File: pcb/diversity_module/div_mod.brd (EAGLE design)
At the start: 40.9 x 28.7 mm, 4 parts

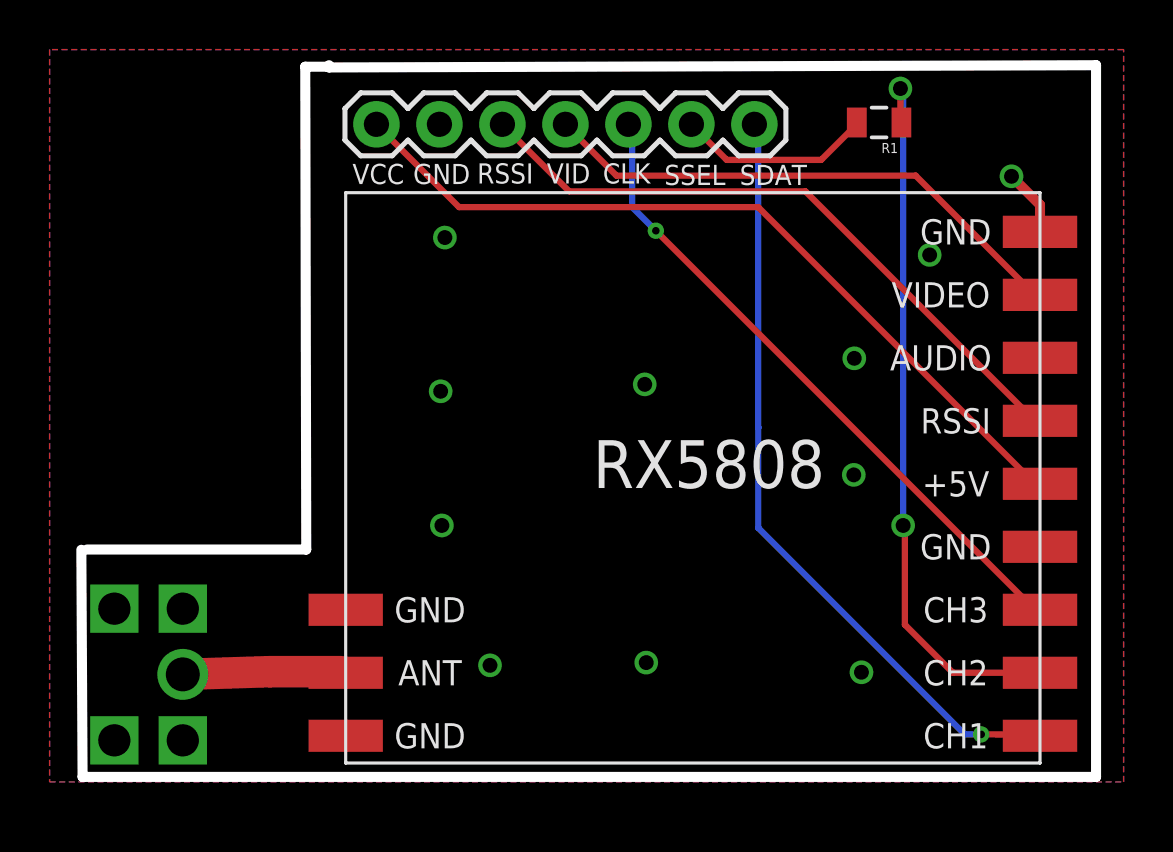
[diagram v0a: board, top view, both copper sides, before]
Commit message: regulator, buffer and new SMA connetor. v1.1
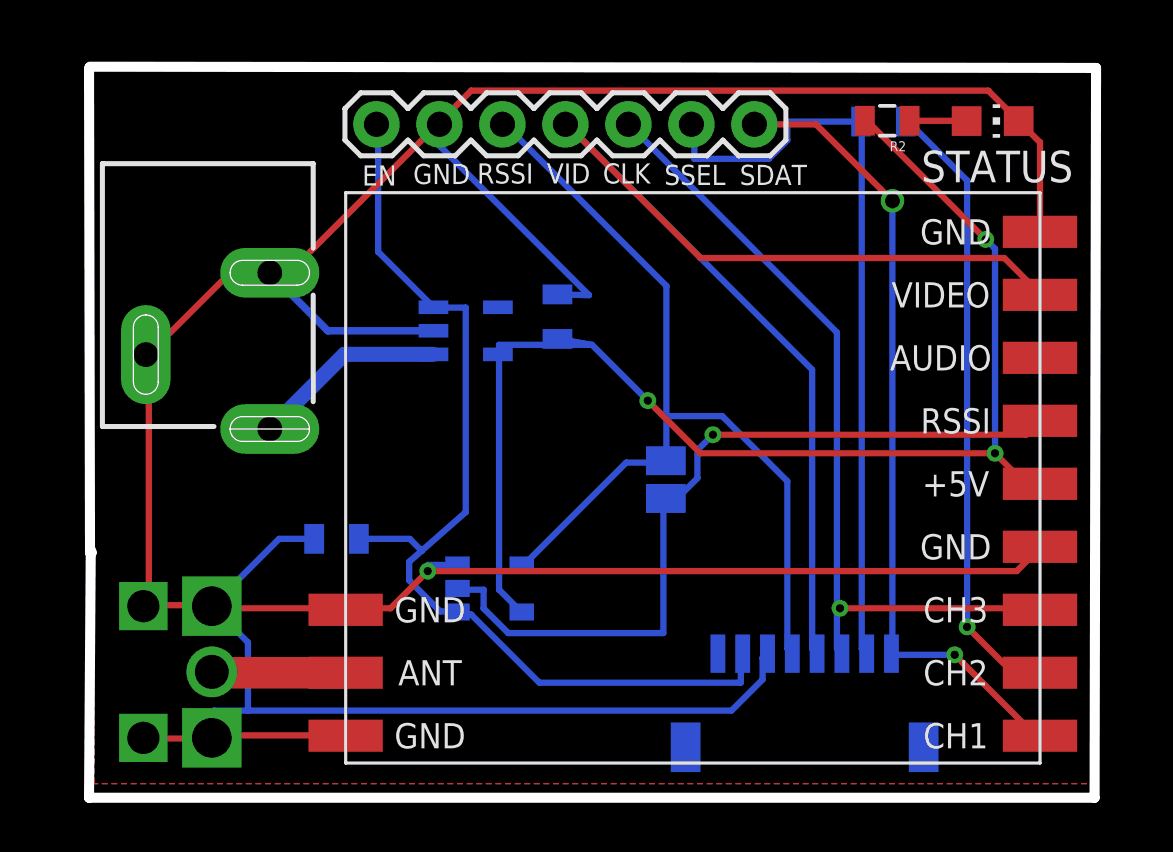
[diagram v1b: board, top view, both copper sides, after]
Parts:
- added C1: 0.1uf, SparkFun-Capacitors:0805
- added IC1: TPS77050, texas:SOT23-DBV
- added IC2: 74AHC1G126DBV, 74xx-little-de:SOT23-5
- added JP1: POWER_JACKSLT, SparkFun-Connectors:POWER_JACK_SLOT
- added R2: (no value), SparkFun-Passives:0805
- added R3: 10k, SparkFun-Passives:0805
- added SJ2: (no value), jumper:SJ
- added STATUS: (no value), led:CHIP-LED0805
- added U$3: EB-85ASMD, SparkFun-Connectors:EB-85A
- moved U$1 1.17 mm to (6.52, 4.41)
- moved R1 0.18 mm to (33.6, 26.6), flipped to the bottom, turned to 0 degrees
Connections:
- new net BATT: U$3.8
- new net ENABLE: IC1.3, IC2.1, JP3.7, R3.2, U$3.7
- new net N$2: R2.1, STATUS.A
- new net RSSI_MOD: IC2.2, RECEIVER_A.RSSI, SJ2.1
- new net VIN_UNREG: IC1.1, JP1.PWR
- net 5V: now also C1.1, IC1.5, IC2.5, R2.2; no longer JP3.7
- net GND: now also C1.2, IC1.2, IC2.3, JP1.GND@1, JP1.GND@2, R3.1, STATUS.C, U$3.6
- net RSSI_B: now also IC2.4, SJ2.2, U$3.5; no longer RECEIVER_A.RSSI
- net RXVIDOUT2: now also U$3.4
- net SPI_CLK: now also U$3.3
- net SPI_DATA: now also U$3.1
- net SPI_SEL_B: now also U$3.2
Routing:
- net GND: track 2.96 -> 155.5 mm, vias 11 -> 1
- net ENABLE: track 0.00 -> 40.7 mm
- net RSSI_MOD: track 0.00 -> 32.6 mm, vias 0 -> 1
- net RXVIDOUT2: track 22.0 -> 47.6 mm
- net SPI_SEL_B: track 7.92 -> 30.8 mm
- net 5V: track 32.8 -> 53.6 mm, vias 0 -> 3
- net RSSI_B: track 26.6 -> 36.9 mm
- net VIN_UNREG: track 0.00 -> 7.85 mm
- net SPI_CLK: track 26.6 -> 33.1 mm
- net N$1: track 29.3 -> 25.2 mm, vias 2 -> 1
- net N$2: track 0.00 -> 2.30 mm
- net SPI_DATA: track 31.2 -> 32.5 mm, vias 1 -> 2
- net N$5: track 6.58 -> 5.41 mm
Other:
- board size 40.9 x 28.7 mm -> 40.6 x 29.5 mm
- board text added: "EN"
- board text added: "buffer_bypass"
- board text added: "mikym0use diversity module v2 part of JAFar project"
- board text removed: "VCC"

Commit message: LDO name replaced
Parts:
- IC1: value TPS77050 -> REG113
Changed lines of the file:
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@@
 <grid distance="0.00999999999" unitdist="mm" unit="mm" style="lines" multiple="1" display="yes" altdistance="0.00500000001" altunitdist="mm" altunit="mm"/>
 <layers>
-<layer number="1" name="Top" color="4" fill="1" visible="yes" active="yes"/>
+<layer number="1" name="Top" color="4" fill="1" visible="no" active="yes"/>
 <layer number="16" name="Bottom" color="1" fill="1" visible="yes" active="yes"/>
 <layer number="17" name="Pads" color="2" fill="1" visible="yes" active="yes"/>
@@
 <attribute name="VALUE" x="24.02" y="3.84" size="1.27" layer="28" rot="MR0"/>
 </element>
-<element name="IC1" library="texas" package="SOT23-DBV" value="TPS77050" x="16.78" y="18.19" smashed="yes" rot="MR90">
-<attribute name="OC_FARNELL" value="1412883" x="16.78" y="18.19" size="1.778" layer="28" rot="MR90" display="off"/>
-<attribute name="OC_NEWARK" value="77C1189" x="16.78" y="18.19" size="1.778" layer="28" rot="MR90" display="off"/>
-<attribute name="MF" value="TEXAS INSTRUMENT CONNECTORS" x="16.78" y="18.19" size="1.778" layer="28" rot="MR90" display="off"/>
-<attribute name="MPN" value="TPS77050DBVT" x="16.78" y="18.19" size="1.778" layer="28" rot="MR90" display="off"/>
+<element name="IC1" library="texas" package="SOT23-DBV" value="REG113" x="16.78" y="18.19" smashed="yes" rot="MR90">
 <attribute name="VALUE" x="19.735" y="20.311" size="1.27" layer="28" rot="MR0"/>
 </element>

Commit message: diversity module v2.0
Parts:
- removed IC1: REG113, texas:SOT23-DBV
- removed IC2: 74AHC1G126DBV, 74xx-little-de:SOT23-5
- removed STATUS: (no value), led:CHIP-LED0805
- added C2: 1uf, SparkFun-Capacitors:0805
- added IC3: OPA336N, burr-brown:SOT23-5
- added JP2: (no value), SparkFun-Connectors:1X02_LOCK
- added SJ1: (no value), jumper:SJ
- added STAT: (no value), led:CHIP-LED0805
- added V1: LP38692P, lp38692:TO252-51
- C1: value 0.1uf -> 1uf
- JP1: value POWER_JACKSLT -> 5.5x2.1mm Barrel; device SparkFun-Connectors:POWER_JACK_SLOT -> SparkFun-Connectors:POWER_JACK_SMD
- moved JP1 24.0 mm to (34.8, 22.4), flipped to the bottom, turned to 270 degrees
- moved R3 13.3 mm to (13.6, 23.0), turned to 0 degrees
- moved SJ2 10.7 mm to (20.9, 2.22), turned to 180 degrees
- moved R1 7.14 mm to (40.7, 25.7), turned to 90 degrees
- moved C1 5.04 mm to (15.7, 20.3), turned to 270 degrees
- moved R2 1.71 mm to (32.1, 27.1), turned to 0 degrees
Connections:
- net 5V: now also IC3.5, SJ1.2, V1.OUT; no longer IC1.5, IC2.5
- net ENABLE: now also SJ1.1, V1.EN; no longer IC1.3, IC2.1
- net GND: now also C2.2, IC3.2, JP1.GND, JP1.P$4, JP2.1, STAT.C, V1.GND; no longer IC1.2, IC2.3, JP1.GND@1, JP1.GND@2, STATUS.C
- net N$2: now also STAT.A; no longer STATUS.A
- net RSSI_B: now also IC3.1, IC3.4; no longer IC2.4
- net RSSI_MOD: now also IC3.3; no longer IC2.2
- net VIN_UNREG: now also C2.1, JP1.VIN0, JP2.2, V1.IN; no longer IC1.1, JP1.PWR
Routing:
- net ENABLE: track 40.7 -> 73.6 mm
- net SPI_CLK: track 33.1 -> 53.0 mm, vias 1 -> 3
- net GND: track 155.5 -> 136.3 mm, vias 1 -> 5
- net SPI_SEL_B: track 30.8 -> 49.5 mm, vias 0 -> 4
- net SPI_DATA: track 32.5 -> 49.4 mm, vias 2 -> 3
- net 5V: track 53.6 -> 64.4 mm, vias 3 -> 2
- net VIN_UNREG: track 7.85 -> 14.9 mm
- net RSSI_MOD: track 32.6 -> 28.0 mm
- net RSSI_B: track 36.9 -> 35.7 mm, vias 0 -> 1
- net RXVIDOUT2: track 47.6 -> 46.9 mm, vias 0 -> 3
- net N$2: track 2.30 -> 1.64 mm
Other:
- board size 40.6 x 29.5 mm -> 40 x 28.9 mm
- board text added: "10k"
- board text added: "470"
- board text added: "VIN"
- board text added: "power"

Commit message: diversity board V2.0
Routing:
- net 5V: track 64.4 -> 67.8 mm
- net GND: vias 5 -> 6
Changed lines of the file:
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@@
 <?xml version="1.0" encoding="utf-8"?>
 <!DOCTYPE eagle SYSTEM "eagle.dtd">
-<eagle version="7.5.0">
+<eagle version="7.4.0">
 <drawing>
 <settings>
@@
 <vertex x="0" y="10.11"/>
 </polygon>
+<via x="25.2" y="13.64" extent="1-16" drill="0.5"/>
 </signal>
 <signal name="SPI_DATA">
@@
 <wire x1="21.082" y1="22.352" x2="21.17" y2="22.59" width="0.254" layer="16"/>
 <wire x1="21.844" y1="11.43" x2="21.844" y2="7.874" width="0.254" layer="16"/>
-<wire x1="14.478" y1="18.796" x2="21.844" y2="11.43" width="0.254" layer="16"/>
 <wire x1="14.478" y1="20.066" x2="14.478" y2="18.796" width="0.254" layer="16"/>
 <wire x1="15.494" y1="21.082" x2="14.478" y2="20.066" width="0.254" layer="16"/>
@@
 <wire x1="25.268" y1="8.65" x2="22.914" y2="8.65" width="0.4064" layer="16"/>
 <wire x1="22.914" y1="8.65" x2="21.95" y2="7.686" width="0.4064" layer="16"/>
+<wire x1="21.844" y1="11.43" x2="15.95" y2="11.43" width="0.254" layer="16"/>
+<wire x1="15.95" y1="11.43" x2="14.46" y2="12.92" width="0.254" layer="16"/>
+<wire x1="14.46" y1="12.92" x2="14.46" y2="18.778" width="0.254" layer="16"/>
+<wire x1="14.46" y1="18.778" x2="14.478" y2="18.796" width="0.254" layer="16"/>
 </signal>
 <signal name="AUDOUT">

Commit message: diversity board v2.1
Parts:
- added R4: 100k, SparkFun-Passives:0805
- moved SJ1 13.8 mm to (13.2, 13.9), turned to 270 degrees
- moved R3 3.87 mm to (13.3, 19.1), turned to 90 degrees
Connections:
- new net ENABLE_P: JP3.7, R4.2, SJ1.1, U$3.7
- net ENABLE: now also R4.1; no longer JP3.7, SJ1.1, U$3.7
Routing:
- net ENABLE_P: track 0.00 -> 64.6 mm
- net ENABLE: track 73.6 -> 9.56 mm
- net 5V: track 67.8 -> 65.4 mm
- net SPI_DATA: track 49.4 -> 48.8 mm
- net GND: track 136.3 -> 135.8 mm, vias 6 -> 8
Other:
- board size 40 x 28.9 mm -> 40 x 29 mm
- board text added: "OPA337"
- board text added: "mikym0use diversity module v2.1 part of JAFar project"
- board text removed: "mikym0use diversity module v2 part of JAFar project"

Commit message: latest from grandparents
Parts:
- removed SJ1: (no value), jumper:SJ
- JP2: device SparkFun-Connectors:1X02_LOCK -> SparkFun-Connectors:1X02
- R3: value 10k -> 100k
- R4: value 100k -> 10k
- moved R1 19.2 mm to (35.5, 7.13)
- moved JP2 0.48 mm to (38.8, 26.3)
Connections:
- net 5V: no longer SJ1.2
- net ENABLE_P: no longer SJ1.1
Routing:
- net GND: track 135.8 -> 96.7 mm, vias 8 -> 7
- net N$1: track 24.9 -> 5.85 mm
- net SPI_SEL_B: track 49.5 -> 41.5 mm, vias 4 -> 1
- net 5V: track 65.4 -> 62.1 mm
- net ENABLE_P: track 64.6 -> 62.7 mm
- net RXVIDOUT2: track 46.9 -> 45.3 mm, vias 3 -> 2
- net SPI_DATA: track 48.8 -> 47.9 mm
- net RSSI_MOD: track 28.0 -> 27.3 mm
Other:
- board text added: "mikym0use diversity module v2.2 part of JAFar project"
- board text removed: "mikym0use diversity module v2.1 part of JAFar project"
- board text removed: "power"
